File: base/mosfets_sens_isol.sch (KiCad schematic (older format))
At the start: 64 parts, among them Q1 КП745А, Q2 КП745А, Q3 КП745А, Q4 КП745А, Q5 КП745А, Q6 КП745А, Q7 КП745А, Q8 КП745А, U1 IR2181, U2 IR2181, U3 IR2181, U4 IR2181, U5 ACS712xLCTR-30A, U6 ACS712xLCTR-30A, U7 ADS7886, U8 ADS7886

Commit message: draf 0.1 of mosfets_sens_isol.sch
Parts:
- removed R? (x3): 100, symbol R
- removed U? (x2): ADuM1400, Housings_SOIC:SOIC-16W_7.5x10.3mm_Pitch1.27mm, symbol ADuM1400
- removed U?: 74HC240, symbol 74HC240
- added C1, C2, C3, C4: 0.1uF, symbol C_Small
- added R17, R18, R19, R20: 33, symbol R
- added U1, U2: SI8640, Package_SOIC:SOIC-16_3.9x9.9mm_P1.27mm, symbol SI8640
- C5: renamed from C1; value 3.3E-7 -> 1uF 50V
- C6: renamed from C2; value 3.3E-7 -> 1uF 50V
- C7: renamed from C3; value 3.3E-7 -> 1uF 50V
- C8: renamed from C4; value 3.3E-7 -> 1uF 50V
- D1, D2, D3, D4: value D -> bav21
- D10, D11, D12, D5, D6, D7, D8, D9: value D -> STTH2R02A
- Q1, Q2, Q3, Q4, Q5, Q6, Q7, Q8: value КП745А -> irf540n
- R10: renamed from R2; value R -> 1
- R11: renamed from R3; value R -> 1
- R12: renamed from R4; value R -> 1
- R13: renamed from R5; value R -> 1
- R14: renamed from R6; value R -> 1
- R15: renamed from R7; value R -> 1
- R16: renamed from R8; value R -> 1
- R9: renamed from R1; value R -> 1
- gave numbers to parts that had none: 8
- renumbered C6 to C10, C7 to C11, C8 to C12, C9 to C13, C10 to C14, C11 to C15, C12 to C16, C13 to C17, C14 to C18, C5 to C9, U8 to U10, U1 to U3, U2 to U4, U3 to U5, U4 to U6, U5 to U7, U6 to U8, U7 to U9
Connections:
- net labels added: +5V
- net labels removed: HIN0_n, HIN1_n, HIN2_n, HIN3_n, LIN0_n, LIN1_n, LIN2_n, LIN3_n
- wire segments 241 -> 239
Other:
- moved on the sheet: C13, C14, C5, C6, C7, C8, D1, D10, D11, D12, D2, D3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

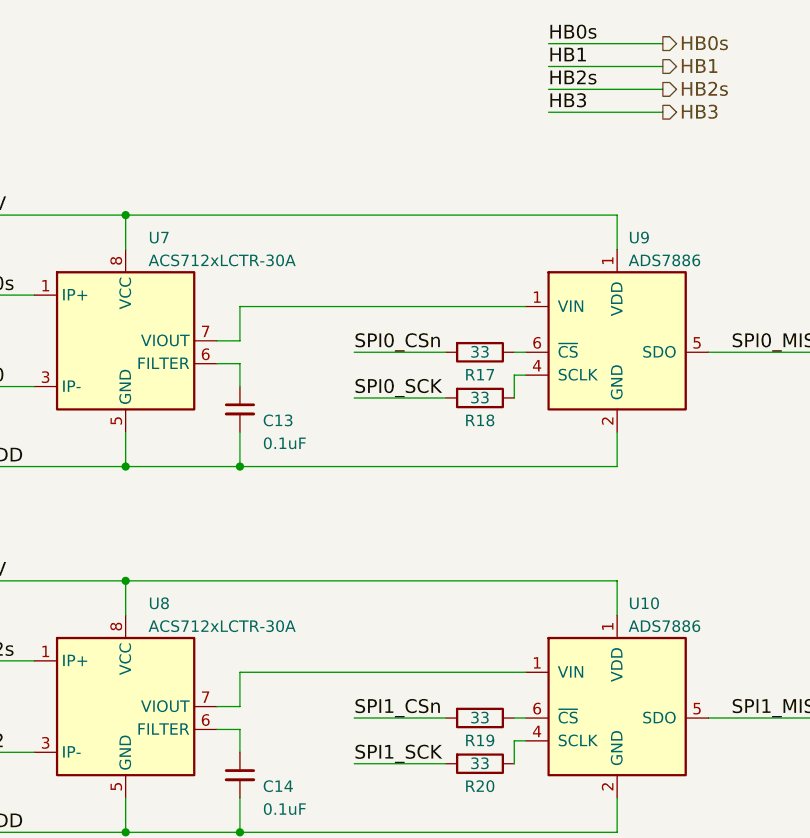
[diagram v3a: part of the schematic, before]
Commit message: Update schematics: 1. Connect analog voltages to MCU board connector 2. Implement Power DC/DC
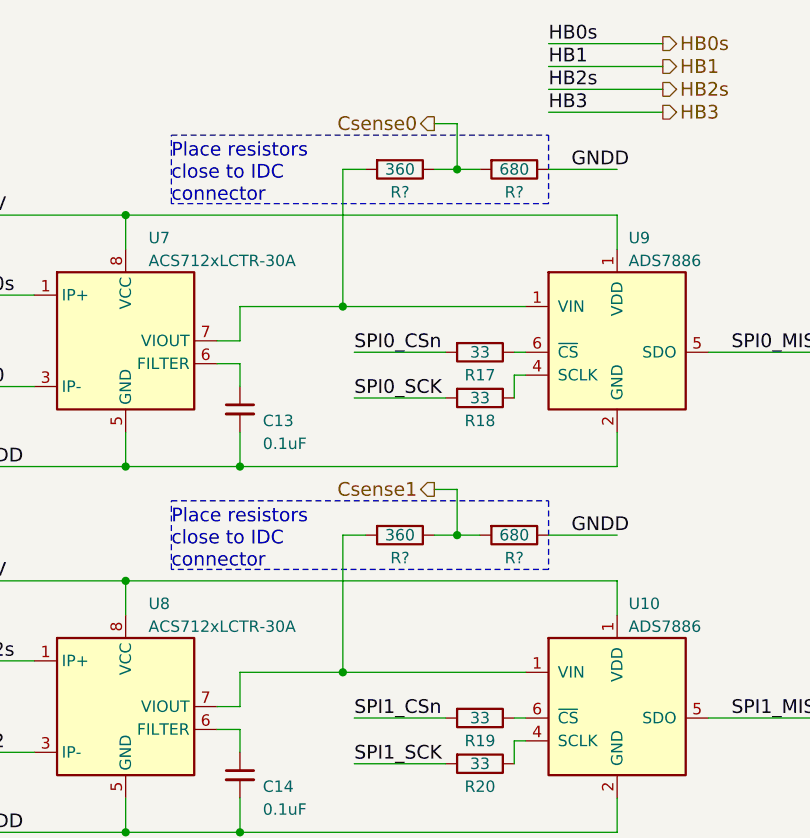
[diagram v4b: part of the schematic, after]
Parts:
- added R? (x2): 360, symbol R
- added R? (x2): 680, symbol R
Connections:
- net labels added: Csense0, Csense1
- wire segments 239 -> 251
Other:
- note added: "Place resistors\nclose to IDC\nconnector"
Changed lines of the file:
@@
 Wire Wire Line
 	9750 3700 9750 3800
+Text HLabel 9400 1000 0    60   Output ~ 0
+Csense0
+Text HLabel 9400 2600 0    60   Output ~ 0
+Csense1
+$Comp
+L R R?
+U 1 1 5A3EBCC5
+P 9250 1200
+F 0 "R?" V 9350 1200 50  0000 C CNN
+F 1 "360" V 9250 1200 50  0000 C CNN
+F 2 "" H 9250 1200 50  0001 C CNN
+F 3 "" H 9250 1200 50  0001 C CNN
+	1    9250 1200
+	0    1    1    0
+$EndComp
+$Comp
+L R R?
+U 1 1 5A3EC054
+P 9750 1200
+F 0 "R?" V 9850 1200 50  0000 C CNN
+F 1 "680" V 9750 1200 50  0000 C CNN
+F 2 "" H 9750 1200 50  0001 C CNN
+F 3 "" H 9750 1200 50  0001 C CNN
+	1    9750 1200
+	0    1    1    0
+$EndComp
+Wire Wire Line
+	9100 1200 9000 1200
+Wire Wire Line
+	9000 1200 9000 1800
+Connection ~ 9000 1800
+Wire Wire Line
+	9400 1200 9600 1200
+Wire Wire Line
+	9500 1200 9500 1000
+Wire Wire Line
+	9500 1000 9400 1000
+Connection ~ 9500 1200
+Wire Wire Line
+	9900 1200 10200 1200
+Text Label 10000 1200 0    60   ~ 0
+GNDD
+Wire Wire Line
+	9500 2600 9400 2600
+Connection ~ 9000 3400
+Text Notes 8250 1350 0    60   ~ 0
+Place resistors\nclose to IDC\nconnector
+Wire Notes Line
+	8250 1050 9900 1050
+Wire Notes Line
+	9900 1050 9900 1350
+Wire Notes Line
+	9900 1350 8250 1350
+Wire Notes Line
+	8250 1350 8250 1050
+$Comp
+L R R?
+U 1 1 5A3EE220
+P 9250 2800
+F 0 "R?" V 9350 2800 50  0000 C CNN
+F 1 "360" V 9250 2800 50  0000 C CNN
+F 2 "" H 9250 2800 50  0001 C CNN
+F 3 "" H 9250 2800 50  0001 C CNN
+	1    9250 2800
+	0    1    1    0
+$EndComp
+$Comp
+L R R?
+U 1 1 5A3EE226
+P 9750 2800
+F 0 "R?" V 9850 2800 50  0000 C CNN
+F 1 "680" V 9750 2800 50  0000 C CNN
+F 2 "" H 9750 2800 50  0001 C CNN
+F 3 "" H 9750 2800 50  0001 C CNN
+	1    9750 2800
+	0    1    1    0
+$EndComp
+Wire Wire Line
+	9100 2800 9000 2800
+Wire Wire Line
+	9000 2800 9000 3400
+Wire Wire Line
+	9400 2800 9600 2800
+Wire Wire Line
+	9500 2800 9500 2600
+Connection ~ 9500 2800
+Wire Wire Line
+	9900 2800 10200 2800
+Text Label 10000 2800 0    60   ~ 0
+GNDD
+Text Notes 8250 2950 0    60   ~ 0
+Place resistors\nclose to IDC\nconnector
+Wire Notes Line
+	8250 2650 9900 2650
+Wire Notes Line
+	9900 2650 9900 2950
+Wire Notes Line
+	9900 2950 8250 2950
+Wire Notes Line
+	8250 2950 8250 2650
 $EndSCHEMATC

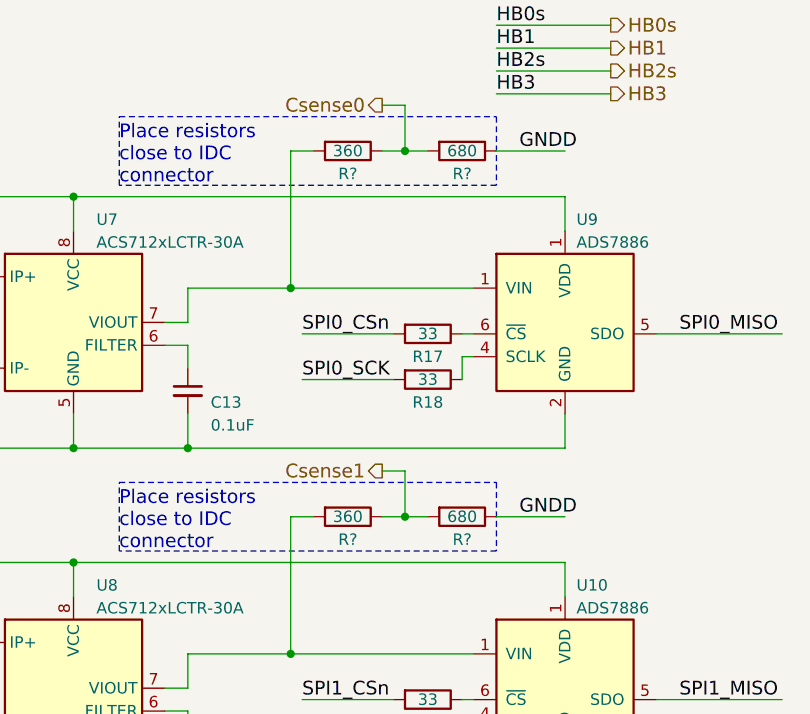
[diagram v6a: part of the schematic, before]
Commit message: Update base board: 1. Add extra analog voltage input to core board.   -> update pinmux 2. Assign most footprints. 3. Generate netlist. 4. Add core_sf board. 5. Add kicad_symbols library submodule.
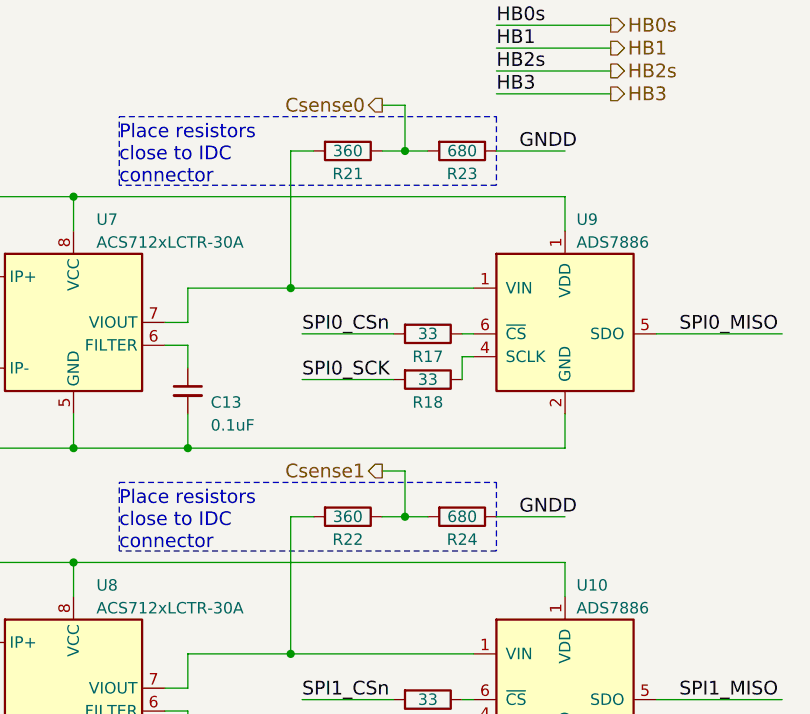
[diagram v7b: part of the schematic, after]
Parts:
- C1, C10, C11, C12, C13, C14, C15, C16, C17, C18, C2, C3, C4, C9: footprint (none) -> Capacitor_SMD:C_0603_1608Metric
- C5, C6, C7, C8: footprint (none) -> Capacitor_SMD:C_0805_2012Metric
- D1, D2, D3, D4: footprint (none) -> Package_TO_SOT_SMD:SOT-23
- D10, D11, D12, D5, D6, D7, D8, D9: footprint (none) -> Diode_SMD:D_SMA
- Q1: footprint (none) -> Package_TO_SOT_THT:TO-220-3_Horizontal
- Q2, Q3, Q4, Q5, Q6, Q7, Q8: footprint (none) -> Package_TO_SOT_THT:TO-220-3_Vertical
- R1, R10, R11, R12, R13, R14, R15, R16, R17, R18, R19, R2, R20, R3, R4, R5, R6, R7, R8, R9: footprint (none) -> Resistor_SMD:R_0603_1608Metric
- R21, R22, R23, R24: renamed from R?; footprint (none) -> Resistor_SMD:R_0603_1608Metric
- U10, U9: footprint TO_SOT_Packages_SMD:SOT-23-6_Handsoldering -> Package_TO_SOT_SMD:SOT-23-6
- U3, U4, U5, U6: footprint (none) -> Package_SOIC:SOIC-8_3.9x4.9mm_P1.27mm
- U7, U8: footprint Housings_SOIC:SOIC-8_3.9x4.9mm_Pitch1.27mm -> Package_SOIC:SOIC-8_3.9x4.9mm_P1.27mm
